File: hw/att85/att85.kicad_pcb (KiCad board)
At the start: 2 copper layers, 80 x 40 mm, 43 parts, among them J101 Barrel_Jack_Switch, J102 Screw_Terminal_01x03, J103 AVR-ISP-6, J104 Conn_01x02, J105 Conn_01x02, Q101 BC817, SW101 SW_Push, SW102 SW_Push, SW103 SW_Push, SW104 SW_Push, SW105 SW_Push, SW106 SW_Push, U101 ATtiny85-20P, U102 MT3608-MODULE, U105 74AHC1G125

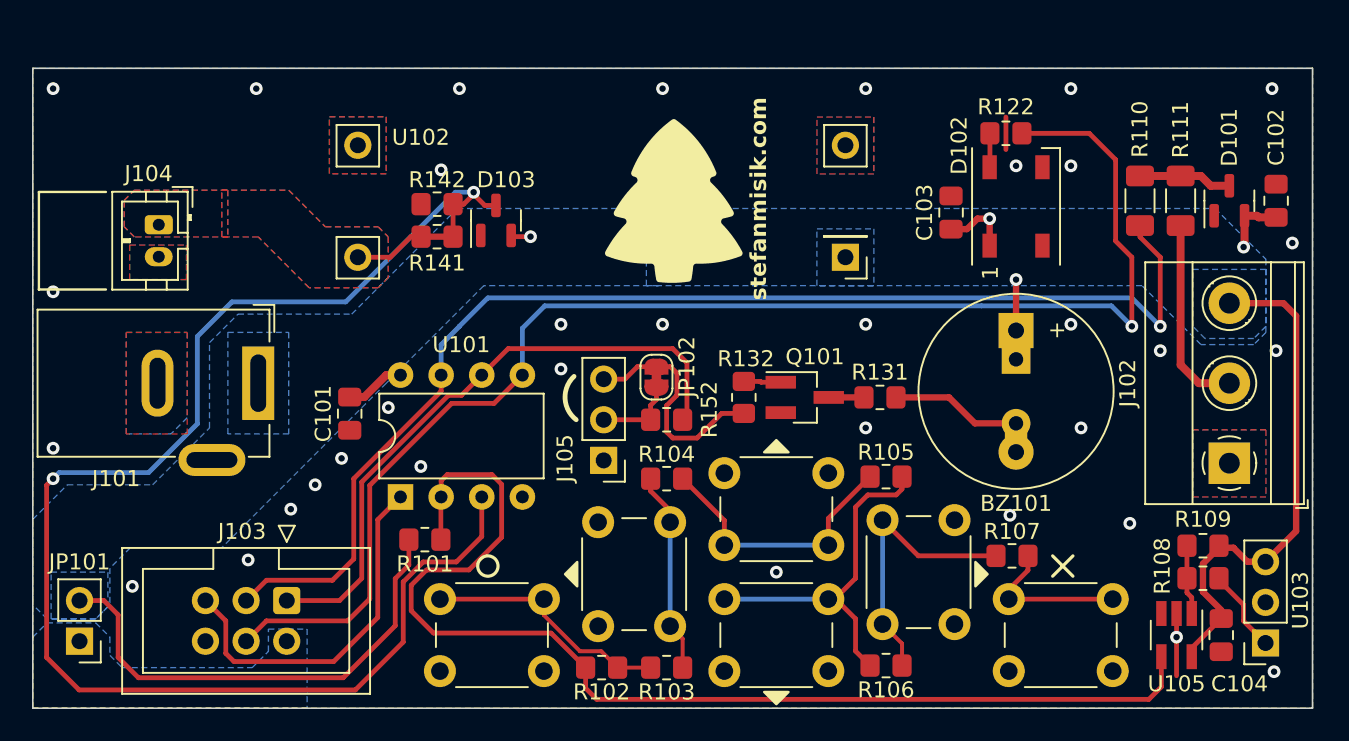
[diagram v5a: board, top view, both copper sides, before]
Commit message: refactor(hw): improve keypad divider layout
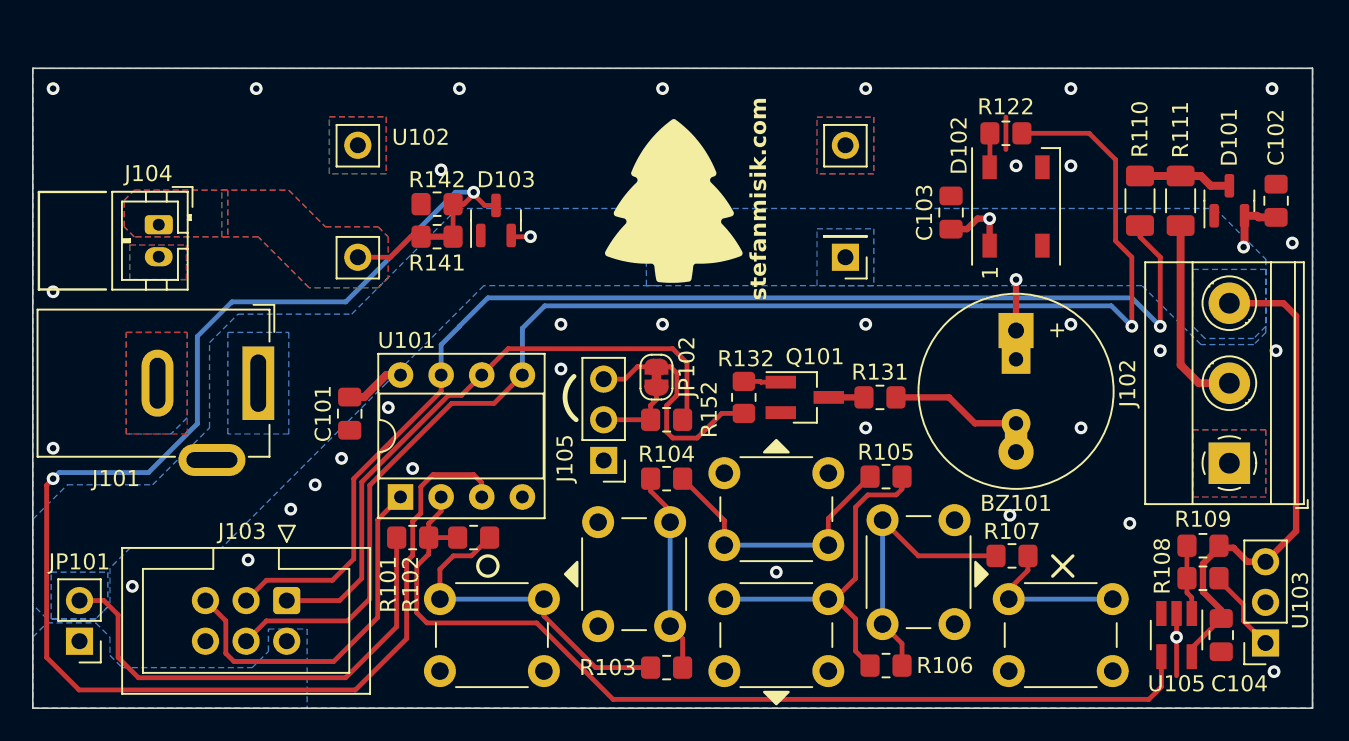
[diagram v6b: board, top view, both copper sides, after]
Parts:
- U101: footprint Package_DIP:DIP-8_W7.62mm -> Package_DIP:DIP-8_W7.62mm_Socket
- moved R102 11.4 mm to (146.9, 104.3)
- moved R101 0.77 mm to (143.1, 104.3)
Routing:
- net /KEYPAD_ADC/IR: track 71.8 -> 60.7 mm
- net Net-(R102-Pad2): track 15.5 -> 21.4 mm
- net /BAT_VMON: track 90.3 -> 93.4 mm

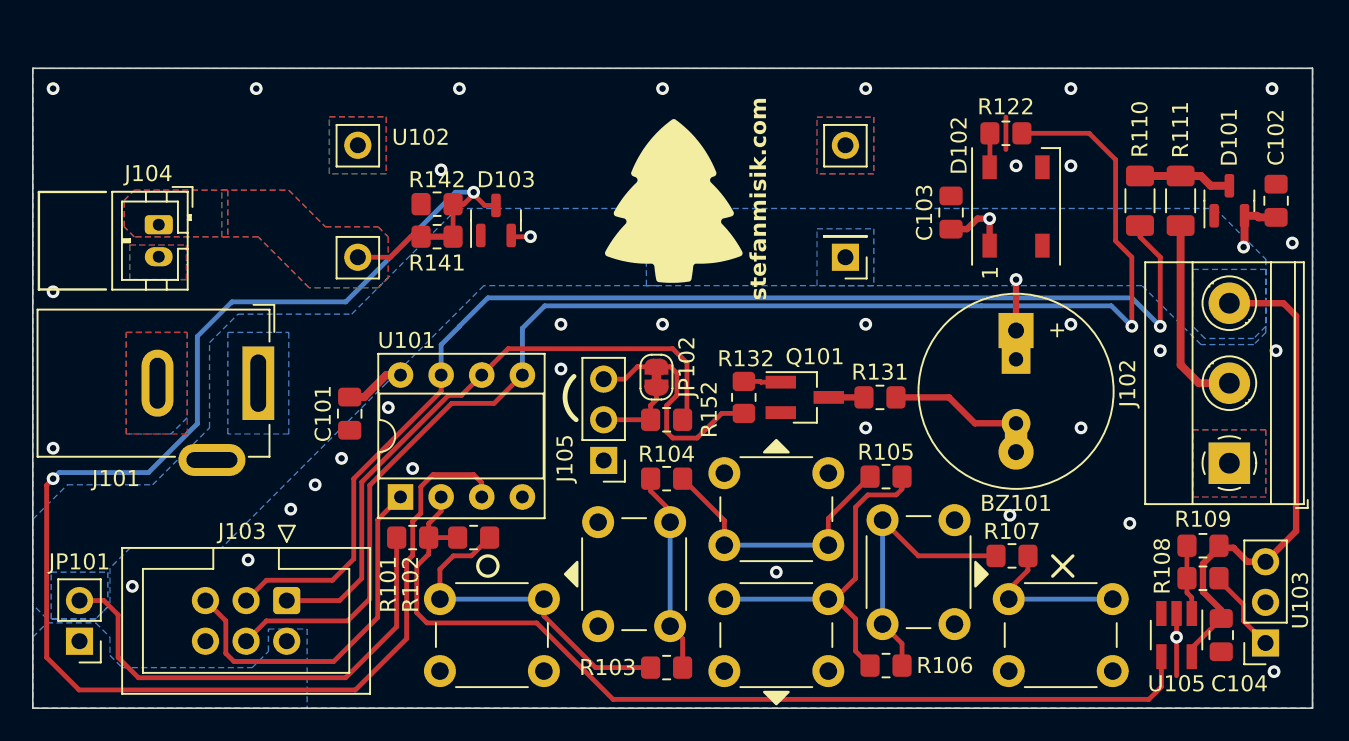
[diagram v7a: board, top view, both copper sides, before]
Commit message: chore(hw): move status LED on main LED DATA, use freed pin for RX
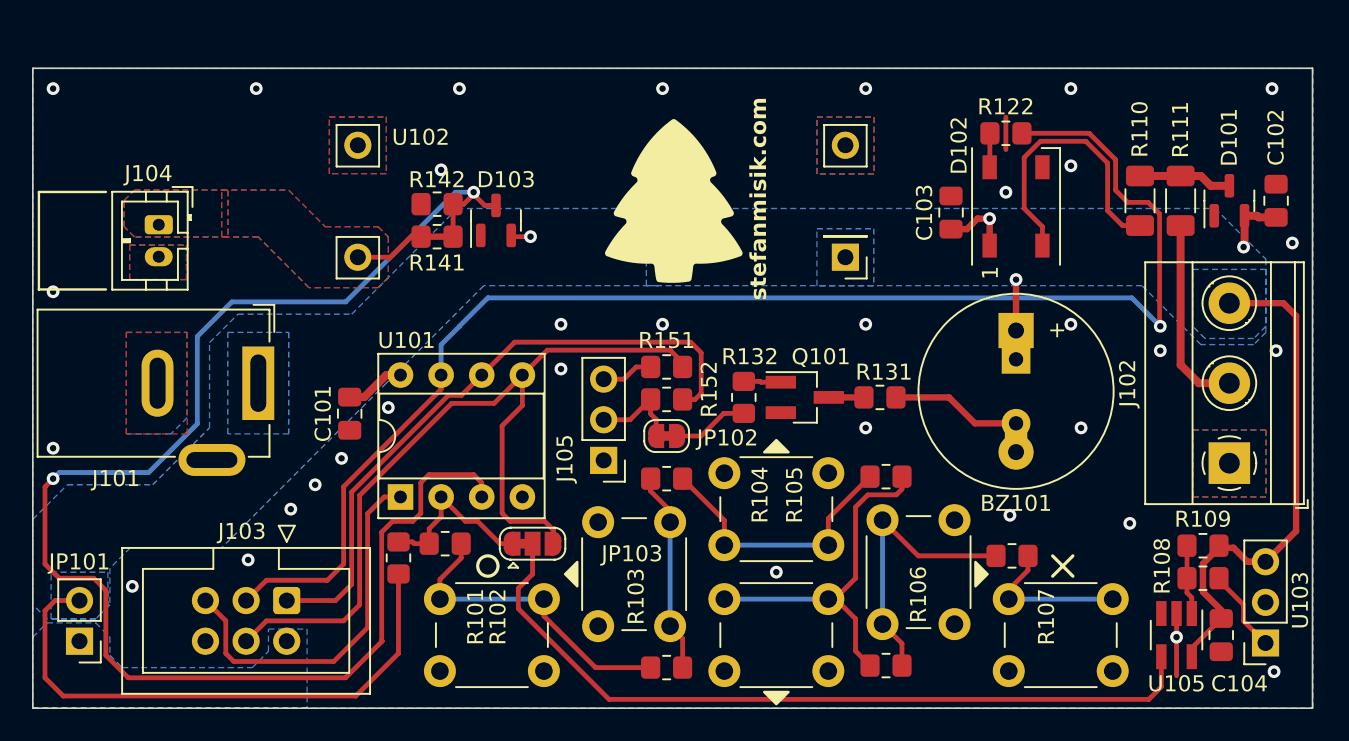
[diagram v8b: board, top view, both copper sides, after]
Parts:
- added JP103: Jumper_3_Bridged12, Jumper:SolderJumper-3_P1.3mm_Bridged12_RoundedPad1.0x1.5mm, F.Cu at (150.6, 104.6)
- added R151: 330R, Resistor_SMD:R_0805_2012Metric_Pad1.20x1.40mm_HandSolder, F.Cu at (159.0, 93.6)
- moved JP102 3.74 mm to (159.0, 97.9), turned to 180 degrees
- moved R102 1.82 mm to (145.2, 104.6)
- moved R101 1.55 mm to (142.2, 105.5), turned to 90 degrees
- moved R152 1.27 mm to (159.0, 95.6)
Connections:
- D102 pad 2: unconnected-(D102-DOUT-Pad2) -> /LED_DATA
- J103 pad 3: /LED_DATA/SCK -> /STATUS/LED_DATA/SCK
- J103 pad 4: /STATUS_LED/MOSI -> /RX/MOSI
- J105 pad 3: /BUZZER -> Net-(J105-Pin_3)
- R110 pad 1: /LED_DATA/SCK -> /LED_DATA
- R122 pad 1: /STATUS_LED/MOSI -> /STATUS/LED_DATA/SCK
- U101 pad 5: /STATUS_LED/MOSI -> /RX/MOSI
- U101 pad 7: /LED_DATA/SCK -> /STATUS/LED_DATA/SCK
- U105 pad 4: /KEYPAD_ADC/IR -> Net-(JP103-C)
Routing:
- net /STATUS/LED_DATA/SCK: track 0.00 -> 89.0 mm, vias 0 -> 1
- net /STATUS_LED/MOSI: track 87.8 -> 0.00 mm, vias 1 -> 0
- net /LED_DATA/SCK: track 77.2 -> 0.00 mm, vias 1 -> 0
- net /RX/MOSI: track 0.00 -> 53.1 mm
- net /KEYPAD_ADC/IR: track 60.7 -> 10.8 mm
- net Net-(JP103-C): track 0.00 -> 49.2 mm
- net /LED_DATA: track 0.00 -> 17.6 mm
- net /BUZZER: track 14.6 -> 4.76 mm
- net +5V: track 79.2 -> 84.2 mm
- net Net-(J105-Pin_3): track 0.00 -> 3.25 mm
- net Net-(R102-Pad2): track 21.4 -> 19.6 mm
- net /BAT_VMON: track 93.4 -> 92.0 mm
- net /BUZZER/TX/MISO: track 39.1 -> 40.1 mm
- net Net-(J105-Pin_2): track 5.11 -> 5.89 mm
- net /RESET: track 22.8 -> 23.4 mm
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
